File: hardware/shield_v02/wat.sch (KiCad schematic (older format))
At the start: 43 parts, among them P1 PINZA_1, P102 CAUDAL_1, P103 V_IN, P106 18b20, P109 LCD_I2C, P110 ARD_DI_06, P111 ARD_ALI_04, P2 PINZA_7, P3 PINZA_2, P4 PINZA_8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

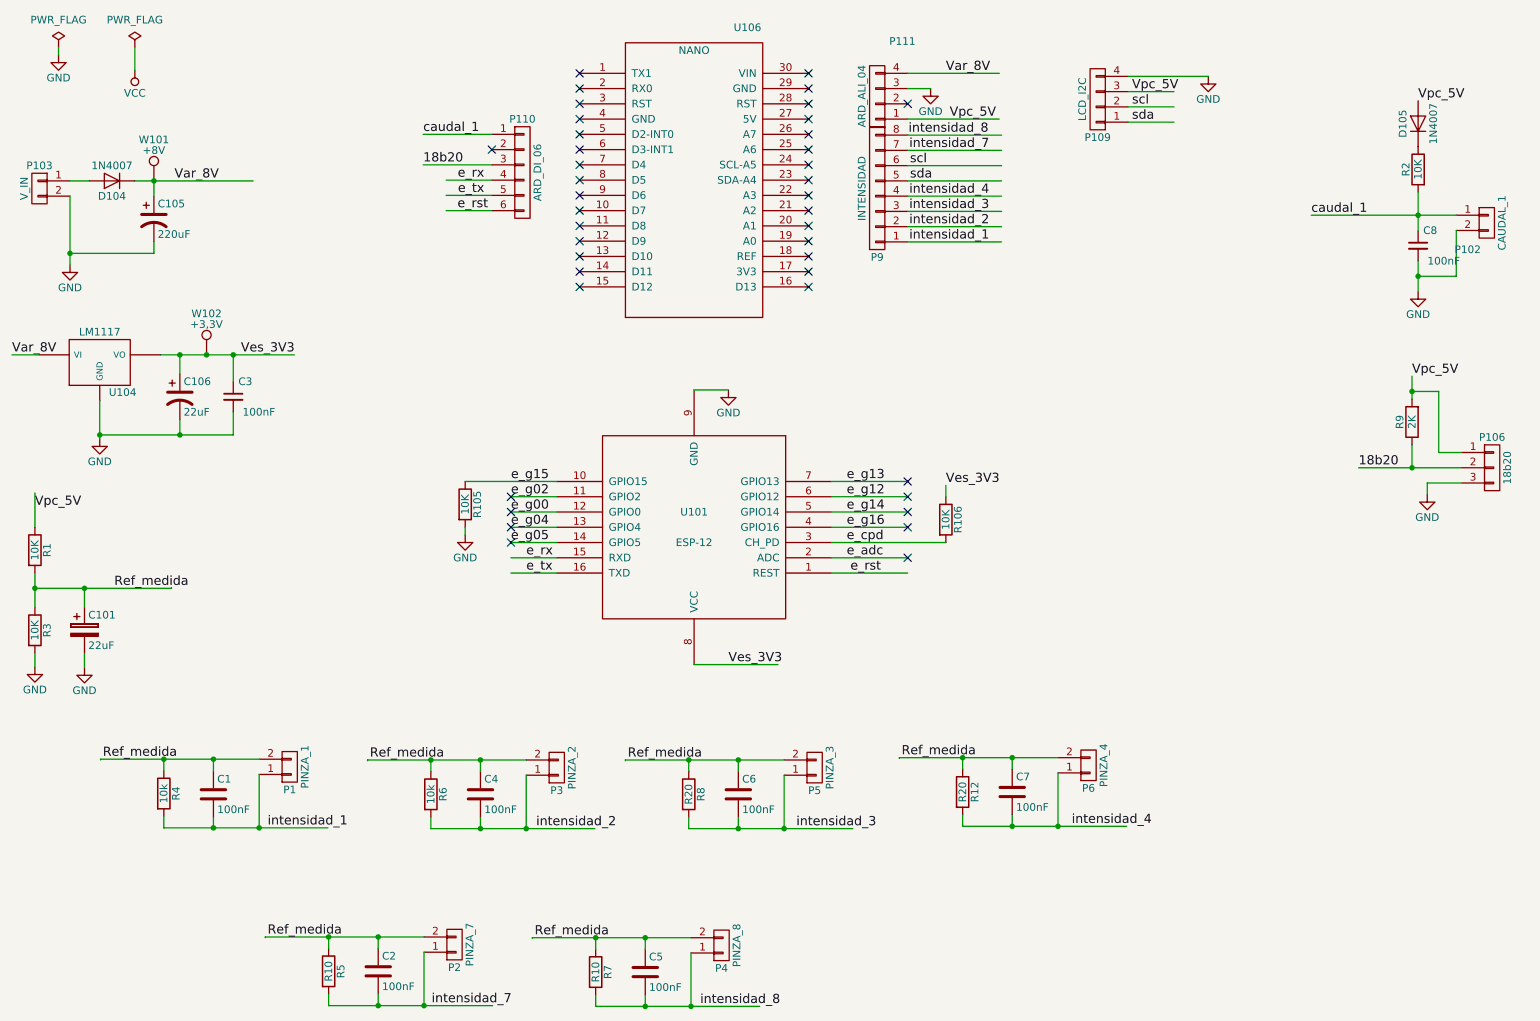
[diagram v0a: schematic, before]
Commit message: pcb cambio de valores de resistencias de carga
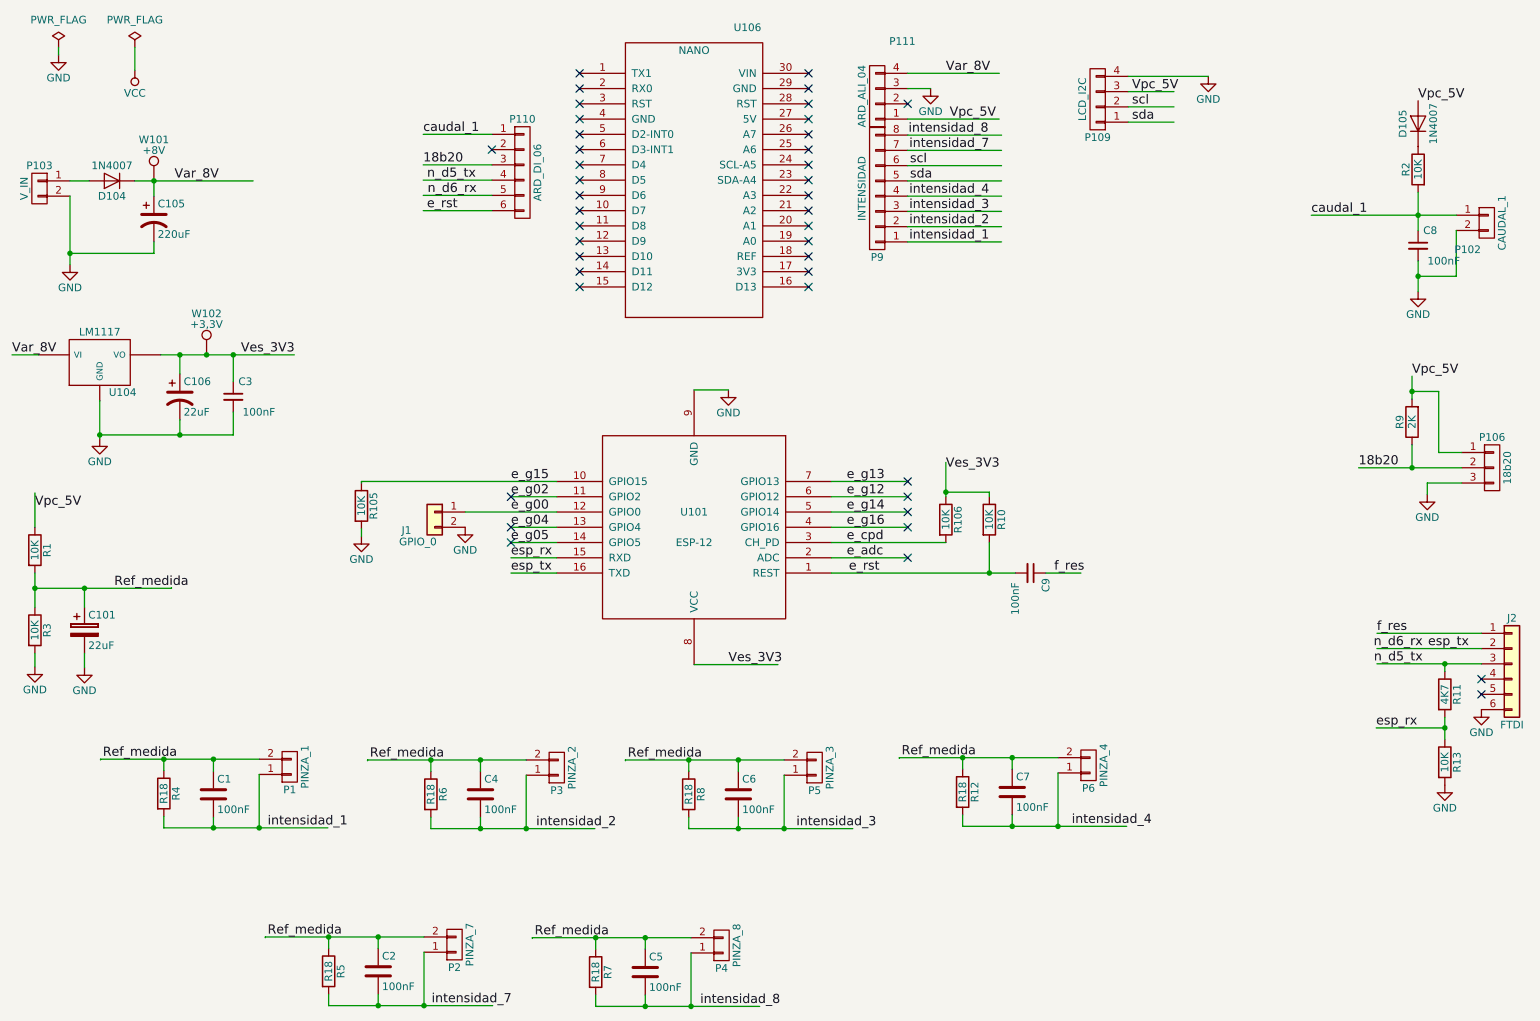
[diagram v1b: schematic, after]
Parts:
- added C9: 100nF, Capacitors_THT:C_Disc_D5.0mm_W2.5mm_P5.00mm, symbol C_Small
- added J1: GPIO_0, Pin_Headers:Pin_Header_Straight_1x02_Pitch2.54mm, symbol Conn_01x02
- added J2: FTDI, Pin_Headers:Pin_Header_Straight_1x06_Pitch2.54mm, symbol Conn_01x06
- added R10, R13: 10K, Resistors_THT:R_Axial_DIN0207_L6.3mm_D2.5mm_P10.16mm_Horizontal, symbol R
- added R11: 4K7, Resistors_THT:R_Axial_DIN0207_L6.3mm_D2.5mm_P10.16mm_Horizontal, symbol R
- R1, R105, R106, R2, R3, R9: footprint Resistors_ThroughHole:Resistor_Horizontal_RM10mm -> Resistors_THT:R_Axial_DIN0207_L6.3mm_D2.5mm_P10.16mm_Horizontal
- R12, R8: value R20 -> R18; footprint Resistors_ThroughHole:Resistor_Horizontal_RM10mm -> Resistors_THT:R_Axial_DIN0207_L6.3mm_D2.5mm_P10.16mm_Horizontal
- R4, R6: value 10k -> R18; footprint Resistors_ThroughHole:Resistor_Horizontal_RM10mm -> Resistors_THT:R_Axial_DIN0207_L6.3mm_D2.5mm_P10.16mm_Horizontal
- R5, R7: value R10 -> R18; footprint Resistors_ThroughHole:Resistor_Horizontal_RM10mm -> Resistors_THT:R_Axial_DIN0207_L6.3mm_D2.5mm_P10.16mm_Horizontal
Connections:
- net labels added: esp_rx, esp_tx, f_res, n_d5_tx, n_d6_rx
- net labels removed: e_rx, e_tx
- wire segments 122 -> 133
- no-connect marks 41 -> 42
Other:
- moved on the sheet: R105
